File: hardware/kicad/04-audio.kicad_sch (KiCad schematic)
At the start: 2 parts, among them U5 PAM8403

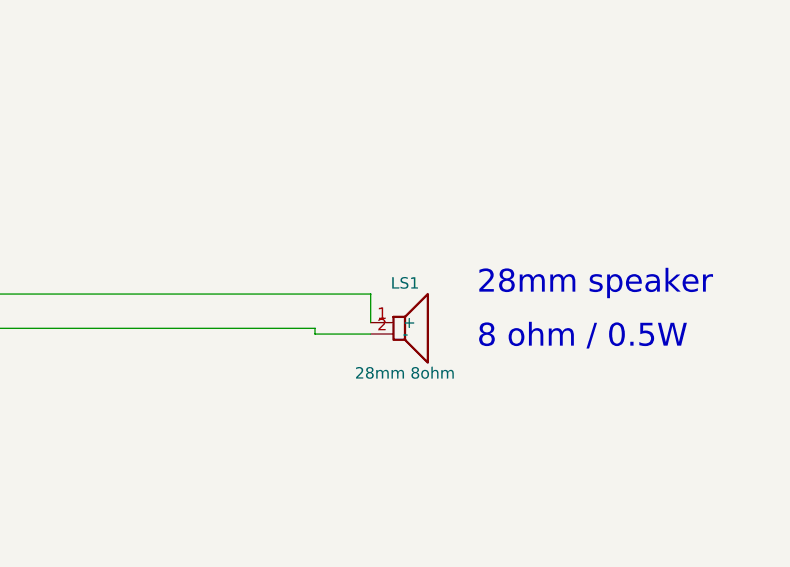
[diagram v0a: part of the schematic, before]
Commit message: Add PCB layout, hierarchical schematics, verification & rendering pipeline
- Reorganize passive components into centered rows below ESP32
- Add missing schematic symbols (LED, FPC_16P, SW_PWR, SW13, SPK1)
- Generate hierarchical root schematic with 7 sub-sheet references
- Create PCB layout generator (4-layer, 160x75mm, JLCPCB-ready)
- Add JLCPCB export (BOM.csv + CPL.csv for 65 components)
- Add schematic/PCB/JLCPCB consistency verification script
- Add PCB SVG renderer + PNG/GIF animation pipeline
- Add interactive 3D PCB viewer (Three.js)
- Update docs (pcb.md, components.md, README.md)

Co-Authored-By: Claude Opus 4.6 <noreply@anthropic.com>
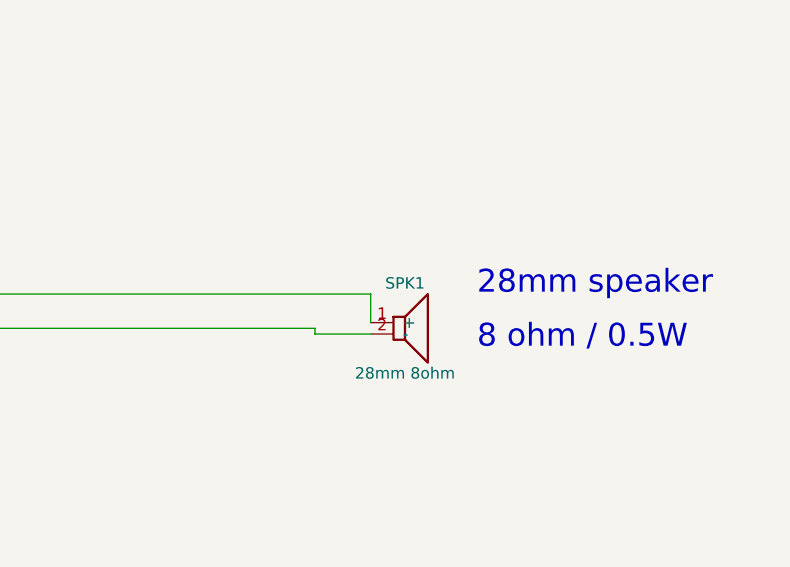
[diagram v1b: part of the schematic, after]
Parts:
- renumbered LS1 to SPK1
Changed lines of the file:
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@@
   (global_label "I2S_DOUT" (shape output) (at 30 88 0) (effects (font (size 1.27 1.27))) (property "Intersheetrefs" "" (at 0 0 0) (effects (font (size 1.27 1.27)) hide)))
   (text "GPIO17 - Serial Data Out -> PAM8403" (at 65 88 0) (effects (font (size 2.54 2.54)) (justify left)))
-  (symbol (lib_id "Speaker") (at 185 110 0) (unit 1) (exclude_from_sim no) (in_bom yes) (on_board yes) (dnp no) (property "Reference" "LS1" (at 185 105 0) (effects (font (size 1.27 1.27)))) (property "Value" "28mm 8ohm" (at 185 115 0) (effects (font (size 1.27 1.27)))) (pin "1") (pin "2"))
+  (symbol (lib_id "Speaker") (at 185 110 0) (unit 1) (exclude_from_sim no) (in_bom yes) (on_board yes) (dnp no) (property "Reference" "SPK1" (at 185 105 0) (effects (font (size 1.27 1.27)))) (property "Value" "28mm 8ohm" (at 185 115 0) (effects (font (size 1.27 1.27)))) (pin "1") (pin "2"))
   (text "28mm speaker" (at 193 105 0) (effects (font (size 2.54 2.54)) (justify left)))
   (text "8 ohm / 0.5W" (at 193 111 0) (effects (font (size 2.54 2.54)) (justify left)))

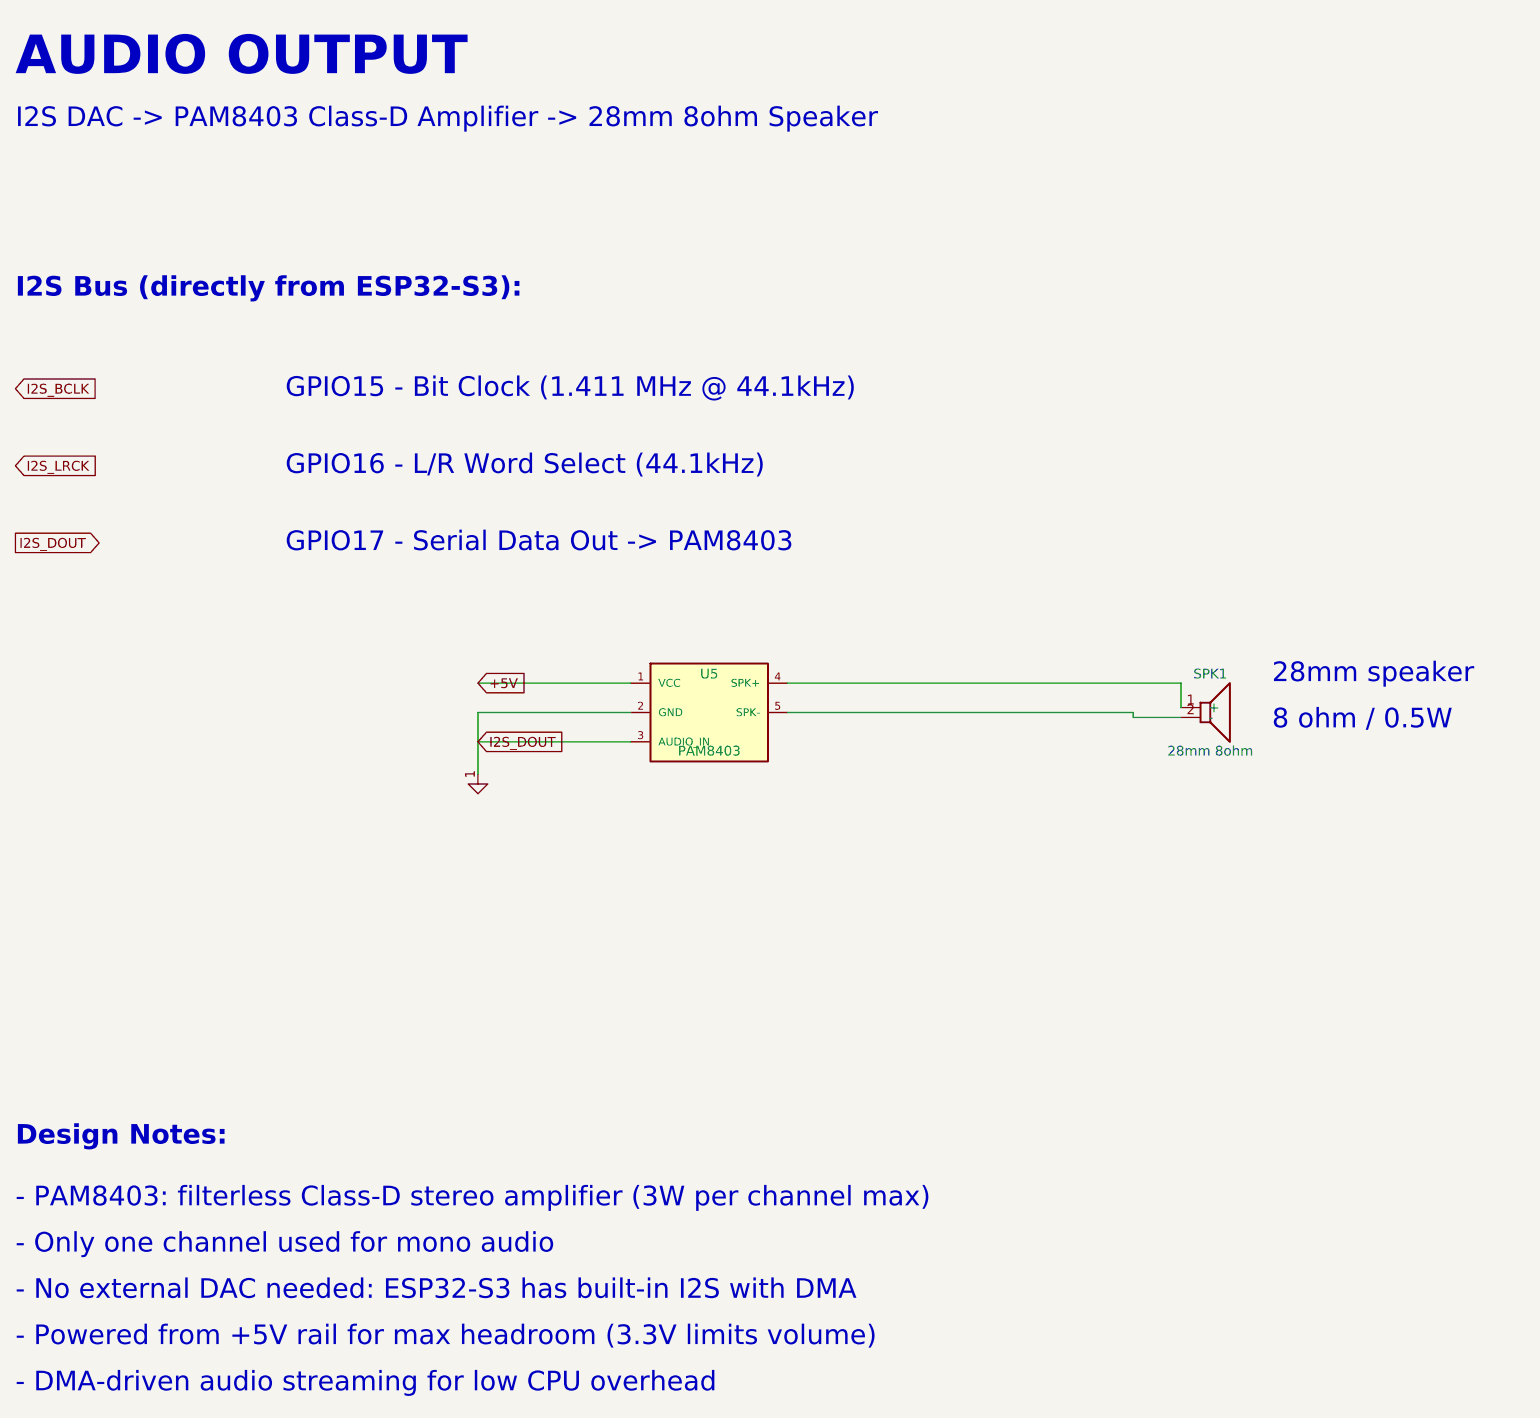
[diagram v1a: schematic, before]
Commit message: fix(schematic): add 7 PAM8403 passives to audio sheet (C21-C25, R20-R21)
Components were in PCB/BOM/CPL but missing from schematic, causing
verify_schematic_pcb.py to report FAIL. All 71 JLCPCB components now
have matching schematic symbols (coverage PASS).

Co-Authored-By: Claude Opus 4.6 (1M context) <noreply@anthropic.com>
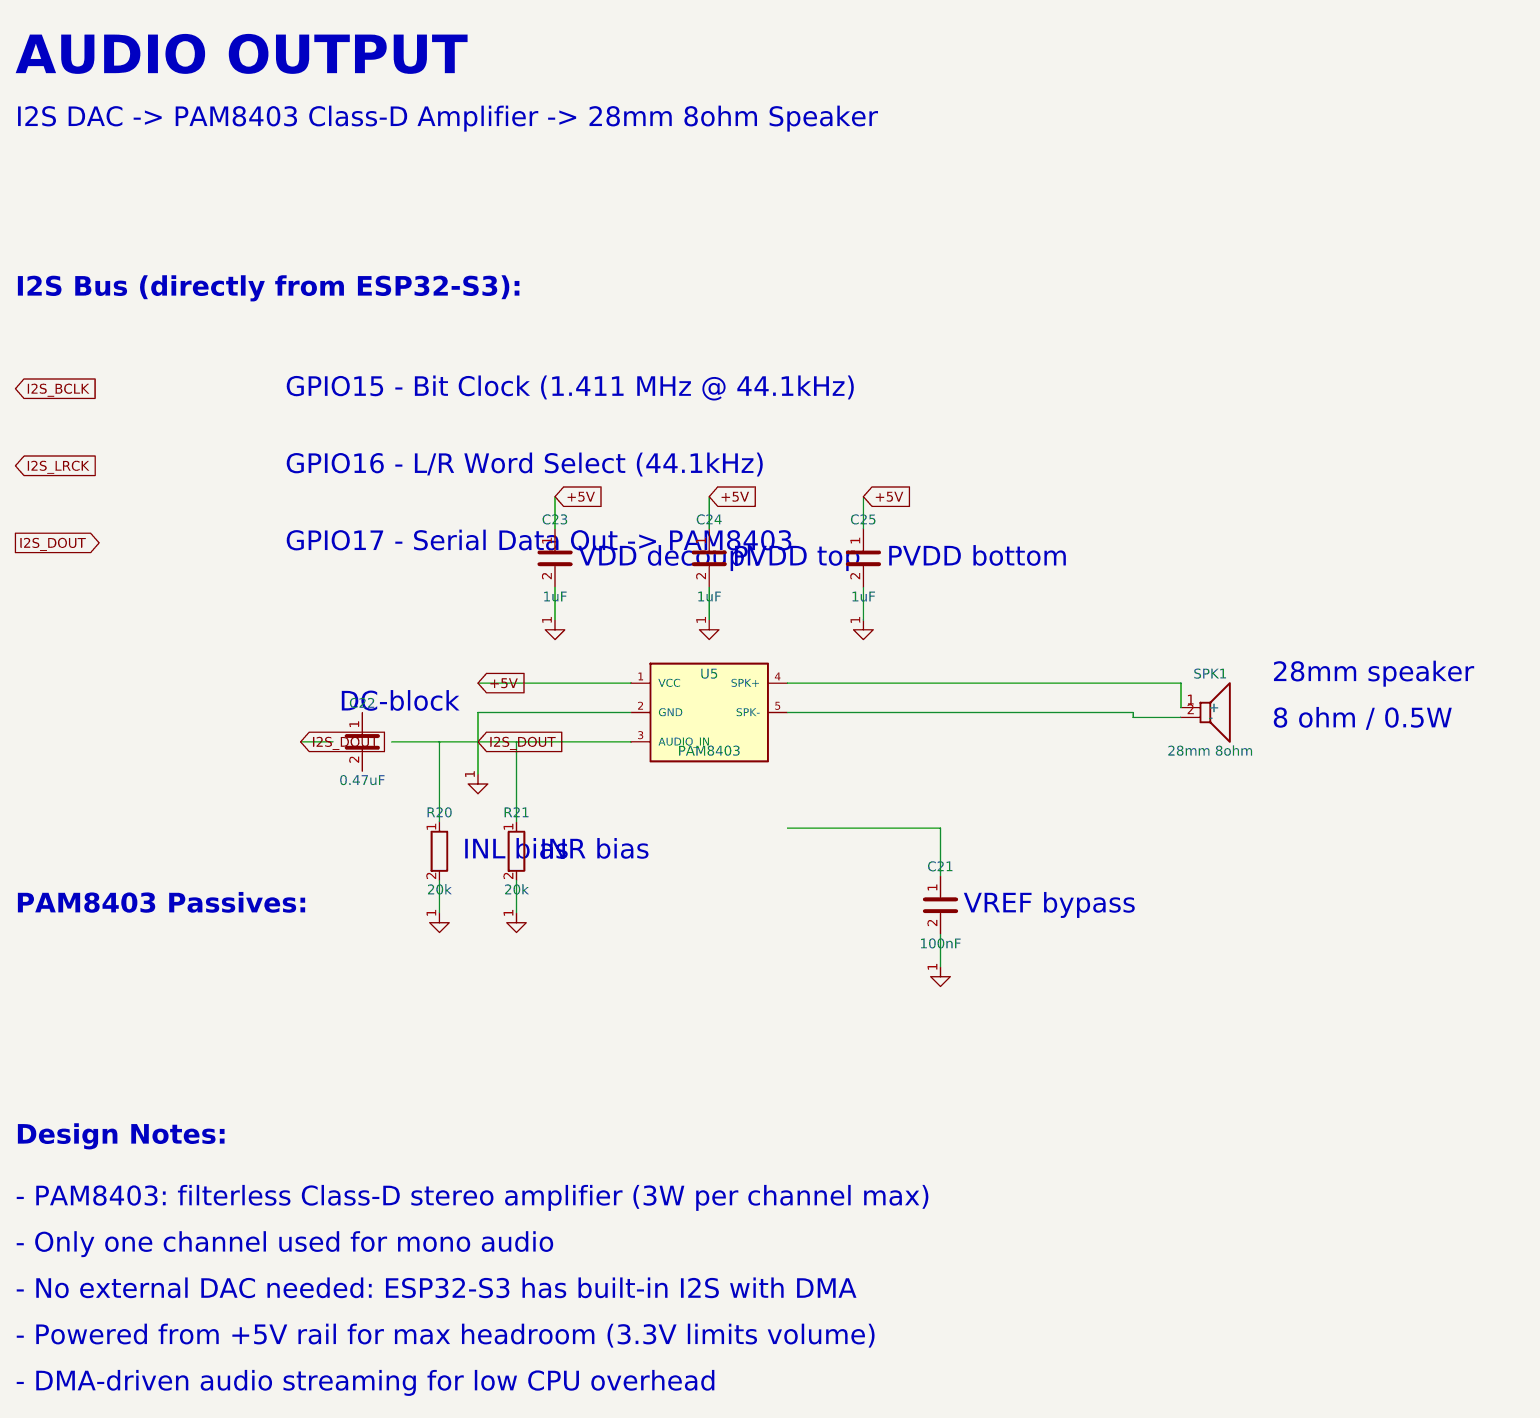
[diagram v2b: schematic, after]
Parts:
- added C21: 100nF, symbol C
- added C22: 0.47uF, symbol C
- added C23, C24, C25: 1uF, symbol C
- added R20, R21: 20k, symbol R
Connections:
- net +5V: now also C23.1, C24.1, C25.1
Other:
- note added: "DC-block"
- note added: "INL bias"
- note added: "INR bias"
- note added: "PAM8403 Passives:"
- note added: "PVDD bottom"
- note added: "PVDD top"
- note added: "VDD decoupl."
- note added: "VREF bypass"
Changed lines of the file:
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@@
   (wire (pts (xy 175 110) (xy 175 110.635)) (stroke (width 0) (type default)))
   (wire (pts (xy 175 110.635) (xy 181.19 110.635)) (stroke (width 0) (type default)))
+  (text "PAM8403 Passives:" (at 30 135 0) (effects (font (size 2.54 2.54) bold) (justify left)))
+  (symbol (lib_id "C") (at 150 135 0) (unit 1) (exclude_from_sim no) (in_bom yes) (on_board yes) (dnp no) (property "Reference" "C21" (at 150 130 0) (effects (font (size 1.27 1.27)))) (property "Value" "100nF" (at 150 140 0) (effects (font (size 1.27 1.27)))) (pin "1") (pin "2"))
+  (wire (pts (xy 150 131.19) (xy 150 125)) (stroke (width 0) (type default)))
+  (wire (pts (xy 150 125) (xy 130.16 125)) (stroke (width 0) (type default)))
+  (symbol (lib_id "GND") (at 150 143 0) (unit 1) (exclude_from_sim no) (in_bom no) (on_board no) (dnp no) (property "Reference" "#PWR002" (at 150 141 0) (effects (font (size 1.27 1.27)) hide)) (property "Value" "GND" (at 150 145 0) (effects (font (size 1.27 1.27)) hide)) (pin "1"))
+  (wire (pts (xy 150 138.81) (xy 150 143)) (stroke (width 0) (type default)))
+  (text "VREF bypass" (at 153 135 0) (effects (font (size 2.54 2.54)) (justify left)))
+  (symbol (lib_id "C") (at 75 113.81 0) (unit 1) (exclude_from_sim no) (in_bom yes) (on_board yes) (dnp no) (property "Reference" "C22" (at 75 108.81 0) (effects (font (size 1.27 1.27)))) (property "Value" "0.47uF" (at 75 118.81 0) (effects (font (size 1.27 1.27)))) (pin "1") (pin "2"))
+  (wire (pts (xy 78.81 113.81) (xy 90 113.81)) (stroke (width 0) (type default)))
+  (wire (pts (xy 71.19 113.81) (xy 67 113.81)) (stroke (width 0) (type default)))
+  (global_label "I2S_DOUT" (shape input) (at 67 113.81 0) (effects (font (size 1.27 1.27))) (property "Intersheetrefs" "" (at 0 0 0) (effects (font (size 1.27 1.27)) hide)))
+  (text "DC-block" (at 72 108.81 0) (effects (font (size 2.54 2.54)) (justify left)))
+  (symbol (lib_id "R") (at 85 128 0) (unit 1) (exclude_from_sim no) (in_bom yes) (on_board yes) (dnp no) (property "Reference" "R20" (at 85 123 0) (effects (font (size 1.27 1.27)))) (property "Value" "20k" (at 85 133 0) (effects (font (size 1.27 1.27)))) (pin "1") (pin "2"))
+  (wire (pts (xy 85 124.19) (xy 85 113.81)) (stroke (width 0) (type default)))
+  (symbol (lib_id "GND") (at 85 136 0) (unit 1) (exclude_from_sim no) (in_bom no) (on_board no) (dnp no) (property "Reference" "#PWR003" (at 85 134 0) (effects (font (size 1.27 1.27)) hide)) (property "Value" "GND" (at 85 138 0) (effects (font (size 1.27 1.27)) hide)) (pin "1"))
+  (wire (pts (xy 85 131.81) (xy 85 136)) (stroke (width 0) (type default)))
+  (text "INL bias" (at 88 128 0) (effects (font (size 2.54 2.54)) (justify left)))
+  (symbol (lib_id "R") (at 95 128 0) (unit 1) (exclude_from_sim no) (in_bom yes) (on_board yes) (dnp no) (property "Reference" "R21" (at 95 123 0) (effects (font (size 1.27 1.27)))) (property "Value" "20k" (at 95 133 0) (effects (font (size 1.27 1.27)))) (pin "1") (pin "2"))
+  (wire (pts (xy 95 124.19) (xy 95 113.81)) (stroke (width 0) (type default)))
+  (symbol (lib_id "GND") (at 95 136 0) (unit 1) (exclude_from_sim no) (in_bom no) (on_board no) (dnp no) (property "Reference" "#PWR004" (at 95 134 0) (effects (font (size 1.27 1.27)) hide)) (property "Value" "GND" (at 95 138 0) (effects (font (size 1.27 1.27)) hide)) (pin "1"))
+  (wire (pts (xy 95 131.81) (xy 95 136)) (stroke (width 0) (type default)))
+  (text "INR bias" (at 98 128 0) (effects (font (size 2.54 2.54)) (justify left)))
+  (symbol (lib_id "C") (at 100 90 0) (unit 1) (exclude_from_sim no) (in_bom yes) (on_board yes) (dnp no) (property "Reference" "C23" (at 100 85 0) (effects (font (size 1.27 1.27)))) (property "Value" "1uF" (at 100 95 0) (effects (font (size 1.27 1.27)))) (pin "1") (pin "2"))
+  (global_label "+5V" (shape input) (at 100 82 0) (effects (font (size 1.27 1.27))) (property "Intersheetrefs" "" (at 0 0 0) (effects (font (size 1.27 1.27)) hide)))
+  (wire (pts (xy 100 86.19) (xy 100 82)) (stroke (width 0) (type default)))
+  (symbol (lib_id "GND") (at 100 98 0) (unit 1) (exclude_from_sim no) (in_bom no) (on_board no) (dnp no) (property "Reference" "#PWR005" (at 100 96 0) (effects (font (size 1.27 1.27)) hide)) (property "Value" "GND" (at 100 100 0) (effects (font (size 1.27 1.27)) hide)) (pin "1"))
+  (wire (pts (xy 100 93.81) (xy 100 98)) (stroke (width 0) (type default)))
+  (text "VDD decoupl." (at 103 90 0) (effects (font (size 2.54 2.54)) (justify left)))
+  (symbol (lib_id "C") (at 120 90 0) (unit 1) (exclude_from_sim no) (in_bom yes) (on_board yes) (dnp no) (property "Reference" "C24" (at 120 85 0) (effects (font (size 1.27 1.27)))) (property "Value" "1uF" (at 120 95 0) (effects (font (size 1.27 1.27)))) (pin "1") (pin "2"))
+  (global_label "+5V" (shape input) (at 120 82 0) (effects (font (size 1.27 1.27))) (property "Intersheetrefs" "" (at 0 0 0) (effects (font (size 1.27 1.27)) hide)))
+  (wire (pts (xy 120 86.19) (xy 120 82)) (stroke (width 0) (type default)))
+  (symbol (lib_id "GND") (at 120 98 0) (unit 1) (exclude_from_sim no) (in_bom no) (on_board no) (dnp no) (property "Reference" "#PWR006" (at 120 96 0) (effects (font (size 1.27 1.27)) hide)) (property "Value" "GND" (at 120 100 0) (effects (font (size 1.27 1.27)) hide)) (pin "1"))
+  (wire (pts (xy 120 93.81) (xy 120 98)) (stroke (width 0) (type default)))
+  (text "PVDD top" (at 123 90 0) (effects (font (size 2.54 2.54)) (justify left)))
+  (symbol (lib_id "C") (at 140 90 0) (unit 1) (exclude_from_sim no) (in_bom yes) (on_board yes) (dnp no) (property "Reference" "C25" (at 140 85 0) (effects (font (size 1.27 1.27)))) (property "Value" "1uF" (at 140 95 0) (effects (font (size 1.27 1.27)))) (pin "1") (pin "2"))
+  (global_label "+5V" (shape input) (at 140 82 0) (effects (font (size 1.27 1.27))) (property "Intersheetrefs" "" (at 0 0 0) (effects (font (size 1.27 1.27)) hide)))
+  (wire (pts (xy 140 86.19) (xy 140 82)) (stroke (width 0) (type default)))
+  (symbol (lib_id "GND") (at 140 98 0) (unit 1) (exclude_from_sim no) (in_bom no) (on_board no) (dnp no) (property "Reference" "#PWR007" (at 140 96 0) (effects (font (size 1.27 1.27)) hide)) (property "Value" "GND" (at 140 100 0) (effects (font (size 1.27 1.27)) hide)) (pin "1"))
+  (wire (pts (xy 140 93.81) (xy 140 98)) (stroke (width 0) (type default)))
+  (text "PVDD bottom" (at 143 90 0) (effects (font (size 2.54 2.54)) (justify left)))
   (text "Design Notes:" (at 30 165 0) (effects (font (size 2.54 2.54) bold) (justify left)))
   (text "- PAM8403: filterless Class-D stereo amplifier (3W per channel max)" (at 30 173 0) (effects (font (size 2.54 2.54)) (justify left)))
